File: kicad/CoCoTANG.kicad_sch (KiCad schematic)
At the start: 108 parts, among them J1 CPU, J10 PIA1_OUT, J13 CoCo_Cart, J14 PIA0_IN, J15 PIA1_IN, J17 AV_IN, J18 CMP_IN, J2 ADDRMUX_OUT, J20 AV_OUT, J21 CMP_OUT, J23 TRG, J28 ADDRMUX, J3 ADDRMUX_IN, J4 PIA0, J5 PIA1, J6 CLK, J7 AV_HEADER, J8 PIA0_OUT, Q1 MMBT3904-TP, Q2 MMBT3904-TP, Q3 MMBT3904-TP, Q4 MMBT3904-TP, Q5 MMBT3904-TP, Q6 MMBT3904-TP, Q7 MMBT3904-TP, Q8 MMBT3904-TP, Q9 MMBT3904-TP, U1 74HC138, U10 74LVC245, U11 74LVC245, U12 74LVC245, U2 AT28C64B-15PU, U22 74HC11, U3 74HC139, U5 Tang_Nano_20k, U7 74HC30, U8 74LVC245, U9 74HC245

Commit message: final board/gerber files
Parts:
- removed C13, C14, C16: 470pF, Capacitor_SMD:C_0805_2012Metric_Pad1.18x1.45mm_HandSolder, symbol Device:C
- removed C15: 1uF, Capacitor_SMD:C_0805_2012Metric_Pad1.18x1.45mm_HandSolder, symbol Device:C
- removed C22: 6.8nF, Capacitor_SMD:C_0805_2012Metric_Pad1.18x1.45mm_HandSolder, symbol Device:C
- removed C23: 4.7uF, Capacitor_SMD:C_0805_2012Metric_Pad1.18x1.45mm_HandSolder, symbol Device:C
- removed C26, C27, C28: 104, Capacitor_SMD:C_0805_2012Metric_Pad1.18x1.45mm_HandSolder, symbol Device:C
- removed J10: PIA1_OUT, Connector_PinHeader_2.54mm:PinHeader_1x02_P2.54mm_Vertical, symbol Connector_Generic:Conn_01x02
- removed J17: AV_IN, Connector_PinHeader_2.54mm:PinHeader_1x06_P2.54mm_Vertical, symbol Connector_Generic:Conn_01x06
- removed J20: AV_OUT, Connector_PinHeader_2.54mm:PinHeader_1x05_P2.54mm_Vertical, symbol Connector_Generic:Conn_01x05
- removed J5: PIA1, FPGA_Common:DIP-40_W15.24mm-OVERSIZED, symbol Connector_Generic:Conn_02x20_Counter_Clockwise
- removed Q1, Q3, Q6: MMBT3904-TP, FPGA_Common:SOT-23_MCC, symbol FPGA_Common:MMBT3904-TP
- removed R13, R14, R15: 75, Resistor_SMD:R_0805_2012Metric_Pad1.20x1.40mm_HandSolder, symbol Device:R
- removed R18, R25, R27, R29, R37, R38, R39: 1K, Resistor_SMD:R_0805_2012Metric_Pad1.20x1.40mm_HandSolder, symbol Device:R
- removed R22: 100K, Resistor_SMD:R_0805_2012Metric_Pad1.20x1.40mm_HandSolder, symbol Device:R
- removed R26, R28, R30: 4.7K, Resistor_SMD:R_0805_2012Metric_Pad1.20x1.40mm_HandSolder, symbol Device:R
- added C17: 1uF, Capacitor_SMD:C_0805_2012Metric_Pad1.18x1.45mm_HandSolder, symbol Device:C
- added JP2: RGB, Jumper:SolderJumper-2_P1.3mm_Open_Pad1.0x1.5mm, symbol Jumper:Jumper_2_Open
- added JP3: PIA0, Jumper:SolderJumper-2_P1.3mm_Open_Pad1.0x1.5mm, symbol Jumper:Jumper_2_Open
- added JP4: PIA1, Jumper:SolderJumper-2_P1.3mm_Open_Pad1.0x1.5mm, symbol Jumper:Jumper_2_Open
- added RN1, RN2: R_Network08, Resistor_THT:R_Array_SIP9, symbol Device:R_Network08
- JP1: value Jumper_2_Open -> AUTOSTART
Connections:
- net PB_33 is gone; now on net B_CHR_33: J18.2 (Pin_2), R33.1
- net PR_33 is gone; now on net R_CVBS_33: J18.3 (Pin_3), R35.1
- net +5V: now also RN1.1 (common), RN2.1 (common)
- net A0: now also RN1.2 (R1)
- net A1: now also RN1.3 (R2)
- net A10: now also RN2.4 (R3)
- net A11: now also RN2.5 (R4)
- net A12: now also RN2.6 (R5)
- net A13: now also RN2.9 (R8)
- net A14: now also RN2.8 (R7)
- net A15: now also RN2.7 (R6)
- net A2: now also RN1.4 (R3)
- net A3: now also RN1.5 (R4)
- net A4: now also RN1.6 (R5)
- net A5: now also RN1.7 (R6)
- net A6: now also RN1.8 (R7)
- net A7: now also RN1.9 (R8)
- net A8: now also RN2.2 (R1)
- net A9: now also RN2.3 (R2)
- net KEYINT: now also J14.3 (Pin_3); no longer J14.1 (Pin_1)
- net SERNT: now also J15.2 (Pin_2); no longer J15.1 (Pin_1)
- net ~{CART}: now also J15.1 (Pin_1); no longer J15.2 (Pin_2)
- net ~{FS}: now also J14.1 (Pin_1); no longer J14.3 (Pin_3), J4.18 (Pin_18), J8.2 (Pin_2)
- net ~{HS}: now also JP3.2 (B); no longer J8.1 (Pin_1)
- net AP10 renamed PB10/SERNT
- net PB10/SERNT: now also JP4.2 (B)
- net CHR_33 renamed B_CHR_33
- net CVBS_33 renamed R_CVBS_33
- net PB_RCA renamed B_CHR
- net B_CHR: now also C17.2, JP2.2 (B); no longer R11.2
- net PR_RCA renamed R_CVBS
- net Y_33 renamed G_Y_33
- net Y_RCA renamed G_Y
- new net: C17.1, JP2.1 (A), R11.2
- new net ~{FS/CART}: J4.18 (Pin_18), J8.1 (Pin_1)
- new net ~{HS}/SERNT: J8.2 (Pin_2), JP3.1 (A), JP4.1 (A)
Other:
- note added: "PIA0 / PIA1 (SC67331/MC6821) DAUGHTERBOARD"
- note removed: "PIA0 (SC67331) DAUGHTERBOARD"
- note removed: "PIA1 (MC6821) DAUGHTERBOARD"
- note removed: "S-VIDEO / CVBS HAT"
- moved on the sheet: C1, C10, C11, C12, C2, C24, C25, C3, C31, C32, C33, C4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

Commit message: update BOM
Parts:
- R19: value 47K -> 4.7K
- RN1, RN2: value R_Network08 -> 4.7K
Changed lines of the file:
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@@
 			)
 		)
-		(property "Value" "R_Network08"
+		(property "Value" "4.7K"
 			(at 319.278 186.6899 0)
 			(show_name no)
@@
 			)
 		)
-		(property "Value" "47K"
+		(property "Value" "4.7K"
 			(at 260.096 183.896 90)
 			(show_name no)
@@
 			)
 		)
-		(property "Value" "R_Network08"
+		(property "Value" "4.7K"
 			(at 288.798 185.9279 0)
 			(show_name no)

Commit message: kicad changes
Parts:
- added C13, C14, C15, C16, C18, C19: 104, Capacitor_SMD:C_0805_2012Metric_Pad1.18x1.45mm_HandSolder, symbol Device:C
- added D4: SS14, Diode_SMD:D_SMA, symbol Device:D_Schottky
- added H1: MountingHole, MountingHole:MountingHole_4.3mm_M4, symbol Mechanical:MountingHole
- added J10: AV_HEADER, Connector_PinSocket_2.54mm:PinSocket_1x06_P2.54mm_Vertical, symbol Connector_Generic:Conn_01x06
- added J11: CLK, Connector_PinSocket_2.54mm:PinSocket_1x01_P2.54mm_Vertical, symbol Connector_Generic:Conn_01x01
- added J12: PIA1_IN, Connector_PinHeader_2.54mm:PinHeader_1x02_P2.54mm_Vertical, symbol Connector_Generic:Conn_01x02
- added J16: PIA0_IN, Connector_PinHeader_2.54mm:PinHeader_1x03_P2.54mm_Vertical, symbol Connector_Generic:Conn_01x03
- added J17: ADDRMUX_IN, Connector_PinHeader_2.54mm:PinHeader_1x07_P2.54mm_Vertical, symbol Connector_Generic:Conn_01x07
- added J19: CPU, FPGA_Common:DIP-40_W15.24mm-OVERSIZED, symbol Connector_Generic:Conn_02x20_Counter_Clockwise
- added J5: EXTKEY, Connector_PinSocket_2.54mm:PinSocket_1x05_P2.54mm_Vertical, symbol Connector_Generic:Conn_01x05
- added J9: EXTKEY_IN, Connector_PinSocket_2.54mm:PinSocket_1x05_P2.54mm_Vertical, symbol Connector_Generic:Conn_01x05
- added Q1, Q3, Q6: MMBT3904-TP, FPGA_Common:SOT-23_MCC, symbol FPGA_Common:MMBT3904-TP
- added R13, R20, R21, R22: 4.7K, Resistor_SMD:R_0805_2012Metric_Pad1.20x1.40mm_HandSolder, symbol Device:R
- added R14, R15, R18: 10K, Resistor_SMD:R_0805_2012Metric_Pad1.20x1.40mm_HandSolder, symbol Device:R
- added R25, R26: 47K, Resistor_SMD:R_0805_2012Metric_Pad1.20x1.40mm_HandSolder, symbol Device:R
- added RN3, RN4: 4.7K, Resistor_THT:R_Array_SIP9, symbol Device:R_Network08
- added SW1: ALT, Button_Switch_Keyboard:SW_Cherry_MX_1.00u_PCB, symbol Switch:SW_Push
- added SW2: CTRL, Button_Switch_Keyboard:SW_Cherry_MX_1.00u_PCB, symbol Switch:SW_Push
- added SW3: F1, Button_Switch_Keyboard:SW_Cherry_MX_1.00u_PCB, symbol Switch:SW_Push
- added SW4: F2, Button_Switch_Keyboard:SW_Cherry_MX_1.00u_PCB, symbol Switch:SW_Push
- added U13, U14, U15, U4: 74LVC245, Package_SO:TSSOP-20_4.4x6.5mm_P0.65mm, symbol FPGA_Common:SN74LVC245AN
- added U16: 74HCT245, Package_SO:TSSOP-20_4.4x6.5mm_P0.65mm, symbol FPGA_Common:SN74LVC245AN
- added U17: Tang_Nano_20k, FPGA_Common:Tang_Nano_20k, symbol Tang20K:Tang_Nano_20k_Audio
- added U6: 74HCT139, Package_SO:TSSOP-16_4.4x5mm_P0.65mm, symbol Connector_Generic:Conn_02x08_Counter_Clockwise
- U1: value 74HC138 -> 74HCT138
- U22: value 74HC11 -> 74HCT11
- U3: value 74HC139 -> 74HCT139
- U7: value 74HC30 -> 74HCT30
- U9: value 74HC245 -> 74HCT245
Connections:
- net +3.3V: now also C14.1, C15.1, C16.1, C18.1, C19.1, J10.5 (Pin_5), R18.1, U13.1 (A->B), U13.20 (VCC), U14.20 (VCC), U15.1 (A->B), U15.20 (VCC), U16.1 (A->B), U17.19 (3V3), U17.25 (3V3), U4.1 (A->B), U4.20 (VCC), U6.16 (Pin_16)
- net +5V: now also U22.5 (Pin_5), C13.1, D4.2 (A), J19.7 (Pin_7), R13.1, RN3.1 (common), RN4.1 (common), U16.20 (VCC)
- net A0: now also J19.8 (Pin_8), RN4.2 (R1), U4.2 (A0)
- net A1: now also J19.9 (Pin_9), RN4.3 (R2), U4.3 (A1)
- net A10: now also J19.18 (Pin_18), RN3.4 (R3), U13.7 (A5)
- net A11: now also J19.19 (Pin_19), RN3.5 (R4), U13.8 (A6)
- net A12: now also J19.20 (Pin_20), RN3.6 (R5), U13.9 (A7)
- net A13: now also J19.21 (Pin_21), RN3.9 (R8), U13.4 (A2)
- net A14: now also J19.22 (Pin_22), RN3.8 (R7), U13.3 (A1)
- net A15: now also J19.23 (Pin_23), RN3.7 (R6), U13.2 (A0)
- net A2: now also J19.10 (Pin_10), RN4.4 (R3), U4.4 (A2)
- net A3: now also J19.11 (Pin_11), RN4.5 (R4), U4.5 (A3)
- net A4: now also J19.12 (Pin_12), RN4.6 (R5), U4.6 (A4)
- net A5: now also J19.13 (Pin_13), RN4.7 (R6), U4.7 (A5)
- net A6: now also J19.14 (Pin_14), RN4.8 (R7), U4.8 (A6)
- net A7: now also J19.15 (Pin_15), RN4.9 (R8), U4.9 (A7)
- net A8: now also J19.16 (Pin_16), RN3.2 (R1), U13.5 (A3)
- net A9: now also J19.17 (Pin_17), RN3.3 (R2), U13.6 (A4)
- net AUDIO_33: now also J10.4 (Pin_4), U16.9 (A7), U17.30 (55_IOR36B)
- net B_CHR_33: now also J10.2 (Pin_2), U17.33 (54_IOR38A)
- net CLK: now also J11.1 (Pin_1), U16.11 (B7)
- net D0: now also J19.31 (Pin_31), U14.18 (B0)
- net D0_33: now also U14.2 (A0), U17.31 (48_IOR49B)
- net D1: now also J19.30 (Pin_30), U14.17 (B1)
- net D1_33: now also U14.3 (A1), U17.29 (49_IOR49A)
- net D2: now also J19.29 (Pin_29), U14.16 (B2)
- net D2_33: now also U14.4 (A2), U17.28 (86_IOT4A)
- net D3: now also J19.28 (Pin_28), U14.15 (B3)
- net D3_33: now also U14.5 (A3), U17.27 (79_IOT27B)
- net D4: now also J19.27 (Pin_27), U14.14 (B4)
- net D4_33: now also U14.6 (A4), U17.24 (72_IOT40B)
- net D5: now also J19.26 (Pin_26), U14.13 (B5)
- net D5_33: now also U14.7 (A5), U17.23 (71_IOT44A)
- net D6: now also J19.25 (Pin_25), U14.12 (B6)
- net D6_33: now also U14.8 (A6), U17.22 (53_IOR38B)
- net D7: now also J19.24 (Pin_24), U14.11 (B7)
- net D7_33: now also U14.9 (A7), U17.21 (52_IOR39A)
- net DATADIR: now also U22.4 (Pin_4), J17.6 (Pin_6), U14.1 (A->B)
- net E: now also J19.34 (Pin_34), R25.1, U16.15 (B3)
- net E_33: now also U16.5 (A3), U17.32 (51_IOR45A)
- net FIRQ_33: now also R15.2, R21.2, U17.3 (75_IOT34A)
- net GND: now also C13.2, C14.2, C15.2, C16.2, C18.2, C19.2, J10.6 (Pin_6), J19.1 (Pin_1), Q1.2, Q3.2, Q6.2, R14.1, R15.1, R25.2, R26.2, U13.10 (GND), U14.10 (GND), U15.10 (GND), U16.10 (GND), U16.19 (CE), U17.20 (GND), U17.26 (GND), U17.39 (GND), U4.10 (GND), U6.1 (Pin_1), U6.8 (Pin_8)
- net G_Y_33: now also J10.1 (Pin_1), U17.34 (56_IOR36A)
- net IRQ_33: now also R14.2, R20.2, U17.17 (19_IOL51A_LED4)
- net KEYINT: now also J16.3 (Pin_3), U15.7 (A5)
- net MP0_33: now also U13.18 (B0), U15.18 (B0), U17.5 (77_IOT30A), U4.18 (B0)
- net MP1_33: now also U13.17 (B1), U15.17 (B1), U17.8 (27_IOB8A), U4.17 (B1)
- net MP2_33: now also U13.16 (B2), U15.16 (B2), U17.9 (28_IOB8B), U4.16 (B2)
- net MP3_33: now also U13.15 (B3), U15.15 (B3), U17.10 (25_IOB6A), U4.15 (B3)
- net MP4_33: now also U13.14 (B4), U15.14 (B4), U17.11 (26_IOB6B), U4.14 (B4)
- net MP5_33: now also U13.13 (B5), U15.13 (B5), U17.12 (29_IOB14A), U4.13 (B5)
- net MP6_33: now also U13.12 (B6), U15.12 (B6), U17.13 (30_IOB14B), U4.12 (B6)
- net MP7_33: now also U13.11 (B7), U15.11 (B7), U17.14 (31_IOB29A), U4.11 (B7)
- net MSEL0: now also U4.19 (CE), U6.4 (Pin_4)
- net MSEL0_33: now also U17.15 (17_IOL49A_LED2), U6.2 (Pin_2)
- net MSEL1: now also U13.19 (CE), U6.5 (Pin_5)
- net MSEL1_33: now also U17.16 (20_IOL51B_LED5), U6.3 (Pin_3)
- net MSEL2: now also U15.19 (CE), U6.6 (Pin_6)
- net PIA0: no longer U22.4 (Pin_4)
- net PIA1: no longer U22.5 (Pin_5)
- net Q: now also J19.35 (Pin_35), R26.1, U16.16 (B2)
- net Q_33: now also U16.4 (A2), U17.38 (76_IOT30B)
- net RESET_33: now also R18.2, R22.2, U17.36 (42_IOB42B)
- net R_CVBS_33: now also J10.3 (Pin_3), U17.18 (18_IOL49B_LED3)
- net R/~{W}: now also J17.7 (Pin_7), J19.32 (Pin_32), R13.2, U15.2 (A0)
- net S0: now also J17.1 (Pin_1), U16.14 (B4)
- net S0_33: now also U16.6 (A4), U17.6 (15_IOL47A_LED0)
- net S1: now also J17.2 (Pin_2), U16.13 (B5)
- net S1_33: now also U16.7 (A5), U17.35 (41_IOB43A)
- net S2: now also J17.3 (Pin_3), U16.12 (B6)
- net S2_33: now also U16.8 (A6), U17.7 (16_IOL47B_LED1)
- net SERNT: now also J12.2 (Pin_2), U15.5 (A3)
- net TSC: now also J19.39 (Pin_39)
- net ~{CART}: now also J12.1 (Pin_1), U15.6 (A4)
- net ~{DATAEN}: now also J17.5 (Pin_5), U14.19 (CE)
- net ~{FIRQ}: now also J19.4 (Pin_4), Q3.3
- net ~{FS_33}: now also U16.2 (A0), U17.2 (74_IOT34B)
- net ~{FS}: now also J16.1 (Pin_1), U16.18 (B0)
- net ~{HALT}: now also J19.40 (Pin_40), U15.8 (A6)
- net ~{HS_33}: now also U16.3 (A1), U17.1 (73_IOT40A)
- net ~{HS}: now also J16.2 (Pin_2), U16.17 (B1)
- net ~{IRQ}: now also J19.3 (Pin_3), Q1.3
- net ~{NMI}: now also J19.2 (Pin_2), U15.9 (A7)
- net ~{RESET}: now also J19.37 (Pin_37), Q6.3, U15.3 (A1)
- net ~{SLENB}: now also J17.4 (Pin_4), U15.4 (A2)
- net AP11 renamed PB1
- net AP12 renamed PB2
- net AP13 renamed PB3
- net PB3: now also J5.2 (Pin_2), J9.2 (Pin_2), SW1.2
- net AP14 renamed PB4
- net PB4: now also J5.3 (Pin_3), J9.3 (Pin_3), SW2.2
- net AP15 renamed PB5
- net PB5: now also J5.4 (Pin_4), J9.4 (Pin_4), SW3.2
- net AP16 renamed PB6
- net PB6: now also J5.5 (Pin_5), J9.5 (Pin_5), SW4.2
- net AP17 renamed PB7
- net AP9 renamed PA7
- net PB10/SERNT renamed PB0
- net ROW0 renamed PA0
- net ROW1 renamed PA1
- net ROW2 renamed PA2
- net ROW3 renamed PA3
- net ROW4 renamed PA4
- net ROW5 renamed PA5
- net ROW6 renamed PA6
- net PA6: now also J5.1 (Pin_1), J9.1 (Pin_1), SW1.1, SW2.1, SW3.1, SW4.1
- new net: Q1.1, R20.1
- new net: D4.1 (K), U17.40 (5V)
- new net: Q3.1, R21.1
- new net: Q6.1, R22.1
- no-connect marks 22 -> 37
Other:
- note added: "26-3134B / 20261058"
- note added: "26-3136 / 20261043"
- note added: "EXTERNAL KEYBOARD EXTENSION"
- note removed: "MAIN BOARD"

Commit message: Go Live
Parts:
- removed J11, J6: CLK, Connector_PinSocket_2.54mm:PinSocket_1x01_P2.54mm_Vertical, symbol Connector_Generic:Conn_01x01
- removed J21: CMP_OUT, Connector_PinHeader_2.54mm:PinHeader_1x05_P2.54mm_Vertical, symbol Connector_Generic:Conn_01x05
- added J11, J20, J22: SUPPORT, Connector_PinSocket_2.54mm:PinSocket_1x02_P2.54mm_Vertical, symbol Connector_Generic:Conn_01x02
- added J24: AV, FPGA_Common:SWITCHCRAFT_57PC5F, symbol Connector:DIN-5_180degree
- added J6: SUPPORT, Connector_PinHeader_2.54mm:PinHeader_1x10_P2.54mm_Vertical, symbol Connector_Generic:Conn_01x10
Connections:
- net AUDIO_33: no longer U16.9 (A7), U9.9 (A7)
- net AUDIO_RCA: now also J24.1
- net B_CHR: now also J24.4
- net GND: now also J24.2
- net G_Y: now also J24.3
- net R_CVBS: now also J24.5
- net CLK: no longer names the net of U9.11 (B7)
- net CLK: no longer U16.11 (B7)
- no-connect marks 37 -> 58
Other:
- moved on the sheet: C24, C25, R23, R24

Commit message: fix some labels
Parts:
- U3, U6: value 74HCT139 -> 74HC139
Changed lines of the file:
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@@
 		(fields_autoplaced yes)
 		(property "Reference" "U6"
-			(at 115.824 383.286 0)
+			(at 115.824 383.54 0)
 			(show_name no)
 			(do_not_autoplace no)
@@
 			)
 		)
-		(property "Value" "74HCT139"
-			(at 115.824 385.826 0)
+		(property "Value" "74HC139"
+			(at 115.824 386.08 0)
 			(show_name no)
 			(do_not_autoplace no)
@@
 			)
 		)
-		(property "Value" "74HCT139"
+		(property "Value" "74HC139"
 			(at 116.586 198.12 0)
 			(show_name no)

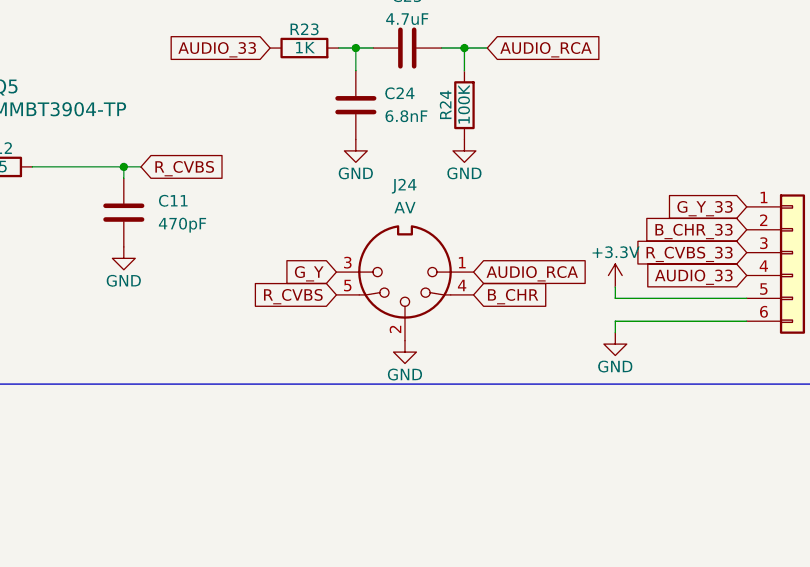
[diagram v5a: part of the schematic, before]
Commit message: change video board DIN position
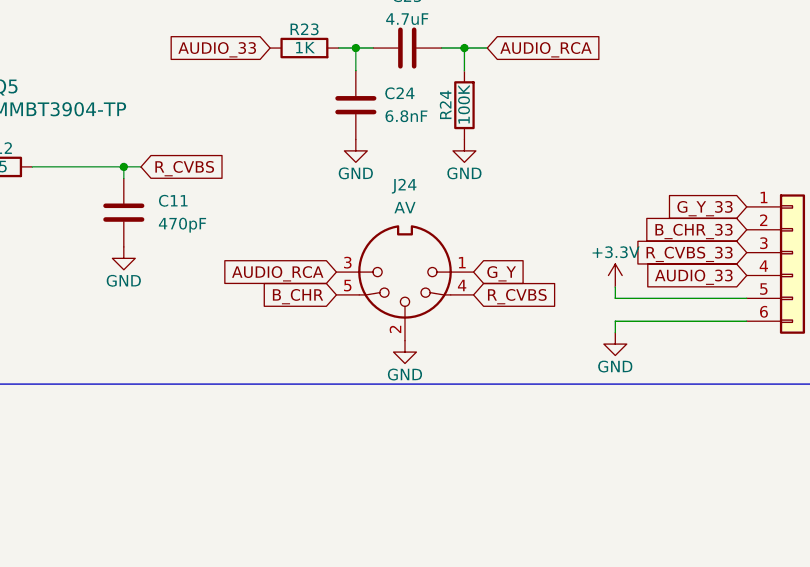
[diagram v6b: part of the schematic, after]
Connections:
- net AUDIO_RCA: now also J24.3; no longer J24.1
- net B_CHR: now also J24.5; no longer J24.4
- net G_Y: now also J24.1; no longer J24.3
- net R_CVBS: now also J24.4; no longer J24.5
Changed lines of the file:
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@@
 	(global_label "AUDIO_RCA"
 		(shape input)
-		(at 612.902 104.394 0)
+		(at 597.662 104.394 180)
 		(fields_autoplaced yes)
 		(effects
@@
 				(size 1.27 1.27)
 			)
-			(justify left)
+			(justify right)
 		)
 		(property "Intersheetrefs" "${INTERSHEET_REFS}"
-			(at 626.1078 104.394 0)
+			(at 584.4562 104.394 0)
 			(hide yes)
 			(show_name no)
@@
 					(size 1.27 1.27)
 				)
-				(justify left)
+				(justify right)
 			)
 		)
@@
 	(global_label "R_CVBS"
 		(shape input)
-		(at 597.662 106.934 180)
+		(at 612.902 106.934 0)
 		(fields_autoplaced yes)
 		(effects
@@
 				(size 1.27 1.27)
 			)
-			(justify right)
+			(justify left)
 		)
 		(property "Intersheetrefs" "${INTERSHEET_REFS}"
-			(at 587.6011 106.934 0)
+			(at 622.9629 106.934 0)
 			(hide yes)
 			(show_name no)
@@
 					(size 1.27 1.27)
 				)
-				(justify right)
+				(justify left)
 			)
 		)
@@
 	(global_label "B_CHR"
 		(shape input)
-		(at 612.902 106.934 0)
+		(at 597.662 106.934 180)
 		(fields_autoplaced yes)
 		(effects
@@
 				(size 1.27 1.27)
 			)
-			(justify left)
+			(justify right)
 		)
 		(property "Intersheetrefs" "${INTERSHEET_REFS}"
-			(at 621.9953 106.934 0)
+			(at 588.5687 106.934 0)
 			(hide yes)
 			(show_name no)
@@
 					(size 1.27 1.27)
 				)
-				(justify left)
+				(justify right)
 			)
 		)
@@
 	(global_label "G_Y"
 		(shape input)
-		(at 597.662 104.394 180)
+		(at 612.902 104.394 0)
 		(fields_autoplaced yes)
 		(effects
@@
 				(size 1.27 1.27)
 			)
-			(justify right)
+			(justify left)
 		)
 		(property "Intersheetrefs" "${INTERSHEET_REFS}"
-			(at 591.3506 104.394 0)
+			(at 619.2134 104.394 0)
 			(hide yes)
 			(show_name no)
@@
 					(size 1.27 1.27)
 				)
-				(justify right)
+				(justify left)
 			)
 		)
